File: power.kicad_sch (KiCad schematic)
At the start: 30 parts, among them IC1 TPS630702RNMR, IC2 RT6150B-33GQW, J1 USB_C_Receptacle_USB2.0_16P, J14 Conn_BATT, U5 MG6206K3B

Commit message: bozza layout pcb
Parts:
- J14: footprint (none) -> Connector_PinHeader_2.54mm:PinHeader_1x02_P2.54mm_Vertical
- L2: footprint (none) -> Inductor_SMD:L_1206_3216Metric_Pad1.42x1.75mm_HandSolder
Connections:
- net -BATT: now also C1.2
- net LX: no longer C1.2
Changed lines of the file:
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@@
 	(text "AOTA-B201610S3R3-101-T\nhttps://mou.sr/3VcfNhi\nhttps://www.lcsc.com/product-detail/C42411119.html?s_z=n_AOTA-B201610S3R3\n\nLEGGERE CAPITOLO 2.1 DEL DATASHEET RP2350 DESIGN\nPER DISPOSIZIONE COMPONENTI!"
 		(exclude_from_sim no)
-		(at 58.928 46.228 0)
+		(at 54.102 50.292 0)
 		(effects
 			(font
@@
 	)
 	(junction
-		(at 64.77 184.15)
+		(at 97.79 43.18)
 		(diameter 0)
 		(color 0 0 0 0)
 	)
 	(junction
-		(at 82.55 26.67)
+		(at 64.77 184.15)
 		(diameter 0)
 		(color 0 0 0 0)
 	)
 	(junction
-		(at 67.31 40.64)
+		(at 82.55 26.67)
 		(diameter 0)
 		(color 0 0 0 0)
@@
 	(wire
 		(pts
-			(xy 67.31 39.37) (xy 67.31 40.64)
-		)
-		(stroke
-			(width 0)
-			(type default)
-		)
-	)
-	(wire
-		(pts
 			(xy 54.61 156.21) (xy 53.34 156.21)
 		)
@@
 	(wire
 		(pts
-			(xy 46.99 40.64) (xy 67.31 40.64)
-		)
-		(stroke
-			(width 0)
-			(type default)
-		)
-	)
-	(wire
-		(pts
 			(xy 38.1 144.78) (xy 54.61 144.78)
 		)
@@
 	(wire
 		(pts
-			(xy 67.31 40.64) (xy 114.3 40.64)
+			(xy 46.99 40.64) (xy 114.3 40.64)
 		)
 		(stroke
@@
 	(wire
 		(pts
+			(xy 67.31 39.37) (xy 67.31 43.18)
+		)
+		(stroke
+			(width 0)
+			(type default)
+		)
+	)
+	(wire
+		(pts
+			(xy 67.31 43.18) (xy 97.79 43.18)
+		)
+		(stroke
+			(width 0)
+			(type default)
+		)
+	)
+	(wire
+		(pts
 			(xy 46.99 30.48) (xy 46.99 31.75)
 		)
@@
 			)
 		)
-		(property "Footprint" ""
+		(property "Footprint" "Connector_PinHeader_2.54mm:PinHeader_1x02_P2.54mm_Vertical"
 			(at 113.03 156.21 0)
 			(effects
@@
 			)
 		)
-		(property "Footprint" ""
+		(property "Footprint" "Inductor_SMD:L_1206_3216Metric_Pad1.42x1.75mm_HandSolder"
 			(at 107.95 137.16 0)
 			(effects

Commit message: L1 footprint updated
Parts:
- L1: footprint Inductor_SMD:L_0805_2012Metric_Pad1.15x1.40mm_HandSolder -> AOTA B201610S3R3-101-T:L_AOTA-B201610S3R3-101-T_MCH
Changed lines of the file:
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@@
 			)
 		)
-		(property "Footprint" "Inductor_SMD:L_0805_2012Metric_Pad1.15x1.40mm_HandSolder"
+		(property "Footprint" "AOTA B201610S3R3-101-T:L_AOTA-B201610S3R3-101-T_MCH"
 			(at 46.99 36.83 0)
 			(effects

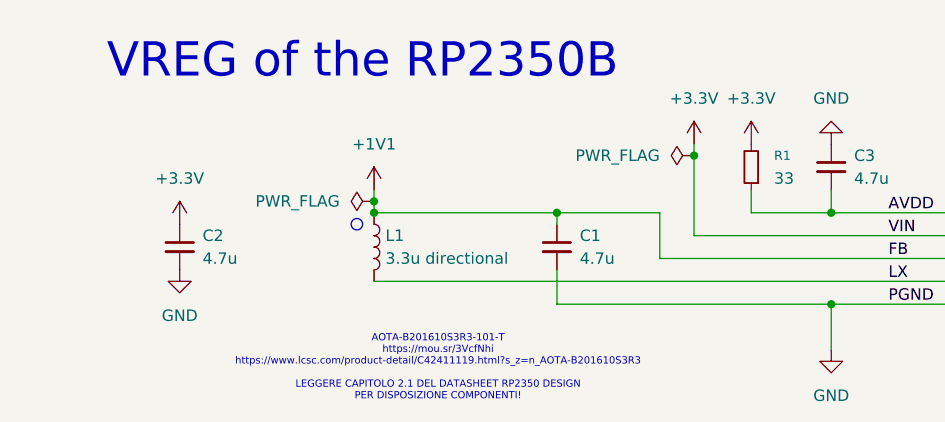
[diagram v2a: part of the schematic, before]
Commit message: NET allignment (all on +3V3)
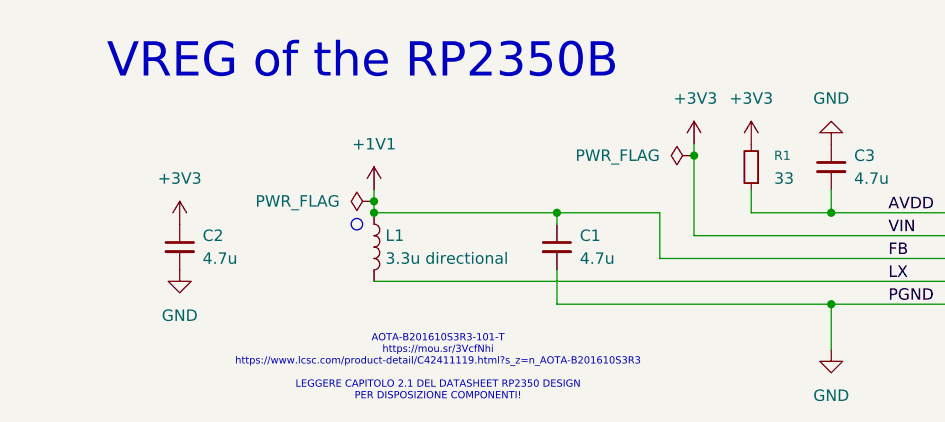
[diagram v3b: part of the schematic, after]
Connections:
- net +3.3V is gone; now on net +3V3: C2.1, R1.2
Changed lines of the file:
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@@
 		(on_board yes)
 		(dnp no)
-		(fields_autoplaced yes)
 		(property "Reference" "#PWR05"
 			(at 82.55 29.21 0)
@@
 			)
 		)
-		(property "Value" "+3.3V"
-			(at 82.55 20.32 0)
-			(effects
-				(font
-					(size 1.27 1.27)
-				)
+		(property "Value" "+3V3"
+			(at 80.264 20.32 0)
+			(effects
+				(font
+					(size 1.27 1.27)
+				)
+				(justify left)
 			)
 		)
@@
 			)
 		)
-		(property "Description" "Power symbol creates a global label with name \"+3.3V\""
+		(property "Description" "Power symbol creates a global label with name \"+3V3\""
 			(at 82.55 25.4 0)
 			(effects
@@
 			)
 		)
-		(property "Value" "+3.3V"
+		(property "Value" "+3V3"
 			(at 25.4 29.21 0)
 			(effects
@@
 			)
 		)
-		(property "Description" "Power symbol creates a global label with name \"+3.3V\""
+		(property "Description" "Power symbol creates a global label with name \"+3V3\""
 			(at 25.4 34.29 0)
 			(effects
@@
 			)
 		)
-		(property "Value" "+3.3V"
+		(property "Value" "+3V3"
 			(at 88.9 20.32 0)
 			(effects
@@
 			)
 		)
-		(property "Description" "Power symbol creates a global label with name \"+3.3V\""
+		(property "Description" "Power symbol creates a global label with name \"+3V3\""
 			(at 88.9 25.4 0)
 			(effects

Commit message: Changes meeting 03/12
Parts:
- removed J14: Conn_BATT, Connector_PinHeader_2.54mm:PinHeader_1x02_P2.54mm_Vertical, symbol Connector:Conn_01x02_Socket
- added J8: 1053141104, CONN_SD-105314-100_04_MOL, symbol Molex_Nanofit:1053141104
- added R41: 10k, Resistor_SMD:R_0603_1608Metric_Pad0.98x0.95mm_HandSolder, symbol Device:R_Small
- added R42: 40k, Resistor_SMD:R_0603_1608Metric_Pad0.98x0.95mm_HandSolder, symbol Device:R_Small
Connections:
- net +BATT: now also J8.3, R42.2
- net -BATT renamed GND
- net GND: now also J8.4, R41.1
- new net BATT_SENSE: R41.2, R42.1

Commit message: changes 20/12
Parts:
- removed C23: 10 uF, symbol Device:C
- removed C24: 20 uF, symbol Device:C
- removed IC2: RT6150B-33GQW, SON50P250X250X80-11N-D, symbol RT6150B-33GQW:RT6150B-33GQW
- removed L3: 2.2 uH, symbol Device:L
- removed R24: 486k, symbol Device:R
- removed R25: 86.6k, symbol Device:R
- removed R26: 10k, symbol Device:R
- removed U5: MG6206K3B, Package_TO_SOT_SMD:TSOT-23_HandSoldering, symbol Regulator_Linear:UA78M33QDCYRQ1
- added C23, C24, C25: C_Small, symbol Device:C_Small
- added L3: L_Small, symbol Device:L_Small
- added R24, R25, R26: R_Small, symbol Device:R_Small
- added U3: L6983NQTR, QFN_NQTR_STM, symbol 2025-12-20_10-01-49:L6983NQTR
- C18, C19: value 1 uF -> 22 uF; footprint (none) -> Capacitor_SMD:C_0603_1608Metric_Pad1.08x0.95mm_HandSolder; now in the parts list
- C22: value 3x22 uF -> 22 uF
- D3, D4: footprint (none) -> SDM2U30CSP:SDM2U30CSP; now in the parts list
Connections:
- net +3V3: now also C18.1, L3.2, R26.1
- net +BATT: no longer C18.1
- net GND: now also C23.2, C24.2, C25.2, R25.1, U3.10 (AGND), U3.3 (A_G_N_D)
- net at D3.1 (K), D4.1 (K): now also C23.1, R24.1, U3.1 (V_I_N), U3.4 (EN/CLKIN)
- new net: L3.1, U3.14 (SW), U3.15 (SW)
- new net: C24.1, R24.2, U3.2 (V_I_N_L_D_O)
- new net: R26.2, U3.5 (PG_OO_D)
- new net: R25.2, U3.8 (FS_W)
- new net: C25.1, U3.9 (VCC)
- no-connect marks 5 -> 4
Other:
- note removed: "DA SCEGLIERE TRA I 3"
- note removed: "MAX 6 V!"
- moved on the sheet: C20, C21, C22, D1, D2, IC1, J8, L2, R20, R21, R22, R23

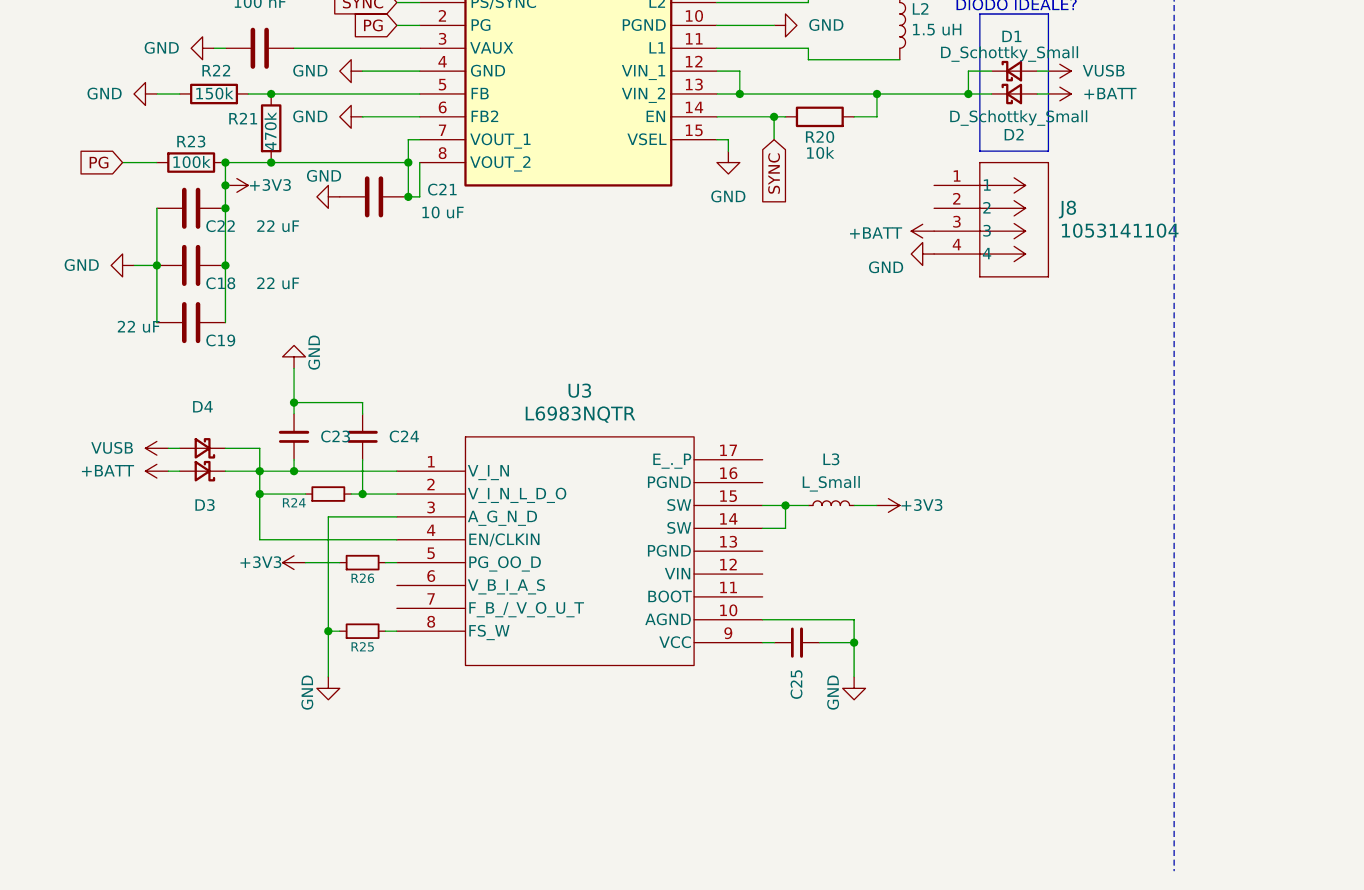
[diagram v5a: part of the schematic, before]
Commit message: Aggiunta regolatore tensione ST
Ho aggiunto il regolatore di tensione ST L6983NQTR, ho fatto le connessioni richieste, ho iniziato il piazzamento dei componenti.
Entro domani in serata dovrei ultimare
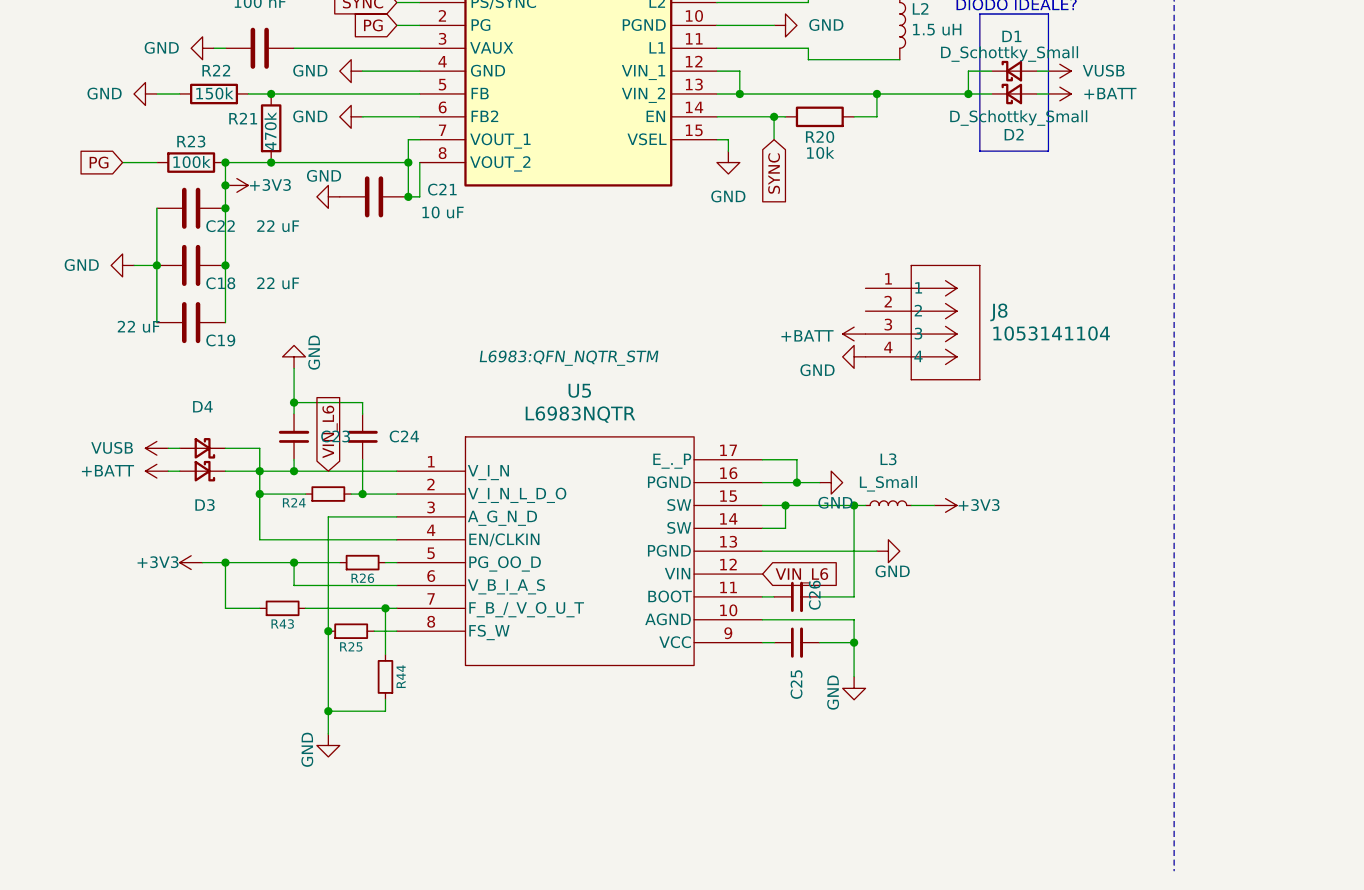
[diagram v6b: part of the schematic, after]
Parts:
- removed U3: L6983NQTR, QFN_NQTR_STM, symbol 2025-12-20_10-01-49:L6983NQTR
- added C26: C_Small, Capacitor_SMD:C_0603_1608Metric_Pad1.08x0.95mm_HandSolder, symbol Device:C_Small
- added R43, R44: R_Small, Resistor_SMD:R_0603_1608Metric_Pad0.98x0.95mm_HandSolder, symbol Device:R_Small
- added U5: L6983NQTR, L6983:QFN_NQTR_STM, symbol 2025-12-20_10-01-49:L6983NQTR
- C23, C24, C25: footprint (none) -> Capacitor_SMD:C_0603_1608Metric_Pad1.08x0.95mm_HandSolder
- L3: footprint (none) -> Inductor_SMD:L_1206_3216Metric_Pad1.42x1.75mm_HandSolder
- R24, R25, R26: footprint (none) -> Resistor_SMD:R_0603_1608Metric_Pad0.98x0.95mm_HandSolder
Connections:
- net +3V3: now also R43.1, U5.6 (V_B_I_A_S)
- net GND: now also R44.1, U5.10 (AGND), U5.13 (PGND), U5.16 (PGND), U5.17 (E_._P), U5.3 (A_G_N_D)
- net VIN_L6: now reaches C23.1, D3.1 (K), D4.1 (K), R24.1
- net VIN_L6: now also U5.1 (V_I_N), U5.12 (VIN), U5.4 (EN/CLKIN)
- net at L3.1: now also C26.2, U5.14 (SW), U5.15 (SW)
- net at C24.1, R24.2: now also U5.2 (V_I_N_L_D_O)
- net at R26.2: now also U5.5 (PG_OO_D)
- net at R25.2: now also U5.8 (FS_W)
- net at C25.1: now also U5.9 (VCC)
- new net: R43.2, R44.2, U5.7 (F_B_/_V_O_U_T)
- new net: C26.1, U5.11 (BOOT)
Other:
- moved on the sheet: J8, L3, R25

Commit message: Ulteriori Modifiche
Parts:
- added C41: C_Small, Capacitor_SMD:C_0603_1608Metric_Pad1.08x0.95mm_HandSolder, symbol Device:C_Small
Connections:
- net GND: now also C41.2
- net VIN_L6: now also C41.1
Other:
- moved on the sheet: C23, C24, R24, R25, R26, R43, R44
